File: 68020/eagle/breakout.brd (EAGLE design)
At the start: 50 x 49.9 mm, 5 parts, among them IC1 MC68020

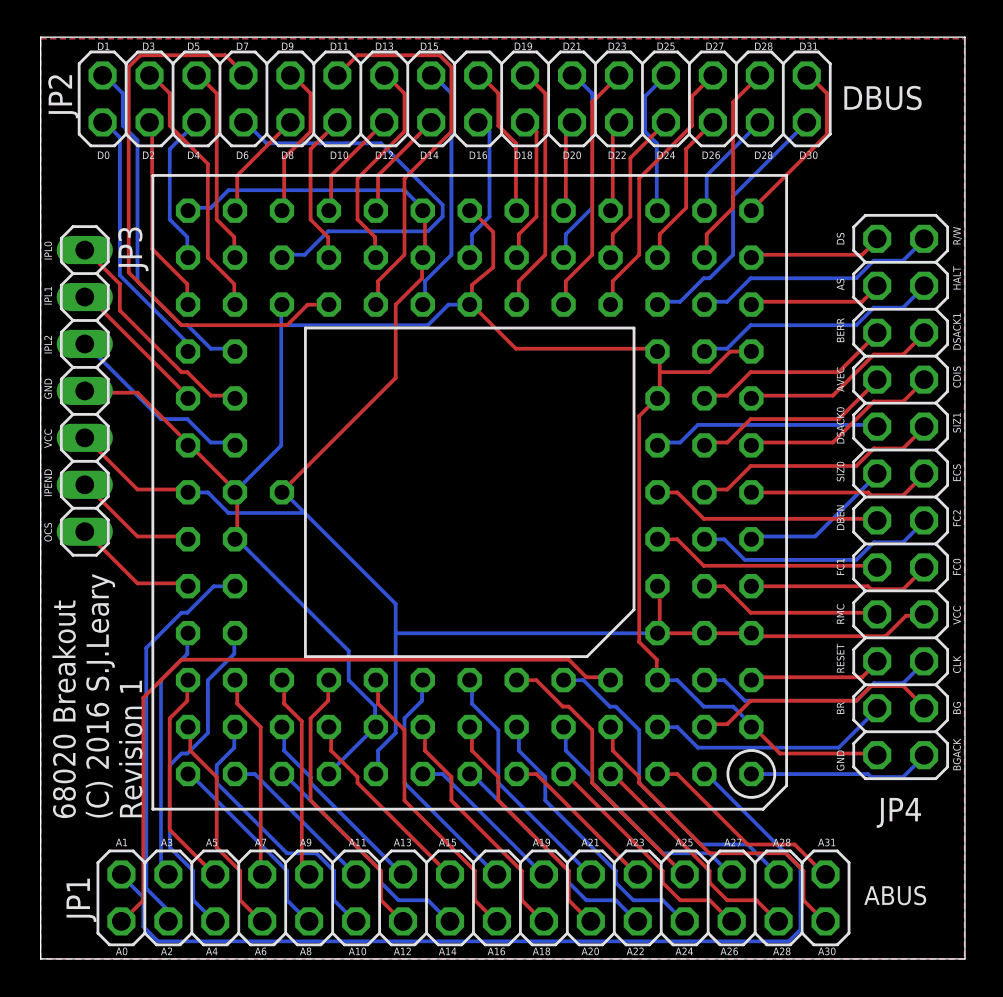
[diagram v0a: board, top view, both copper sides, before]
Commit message: refactored 68020 breakout board to be a mirror of the 030 board... means they can mate. Added an unrouted shunt for the 68k
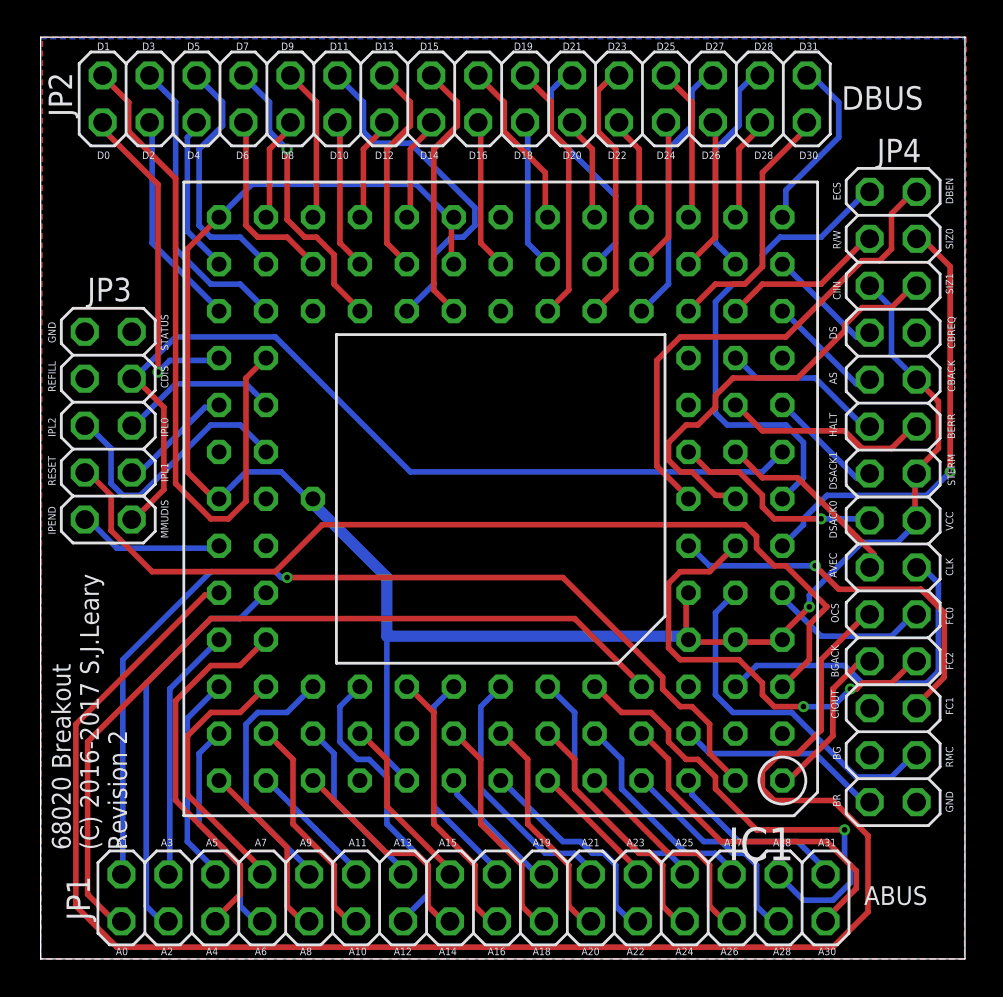
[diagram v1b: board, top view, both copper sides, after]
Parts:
- IC1: value MC68020 -> (none)
- JP3: value IPL BUS -> (none); device pinhead:1X07 -> pinhead:2X05
- JP4: device pinhead:2X12 -> pinhead:2X14
- moved JP3 2.27 mm to (3.66, 28.9)
- moved IC1 1.71 mm to (24.9, 24.9)
- moved JP4 0.41 mm to (46.1, 25.0)
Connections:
- new net BG: IC1.B02
- new net CBREQ: JP4.8
- new net CIIOUT: JP4.23
- new net REFILL: JP3.3
- new net STATUS: JP3.2
- net AS20: now also JP4.9; no longer JP4.3
- net AVEC: now also JP4.17; no longer JP4.7
- net BERR: now also JP4.12; no longer JP4.5
- net BG20: now also JP4.25; no longer IC1.B02, JP4.22
- net BGACK: now also JP4.21; no longer JP4.24
- net BR: now also JP4.27; no longer JP4.21
- net CDIS: now also JP3.10, JP3.4; no longer JP4.8
- net CLK20: now also JP4.18; no longer JP4.20
- net DBEN: now also JP4.2; no longer JP4.13
- net DS20: now also JP4.7; no longer JP4.1
- net DSACK0: now also JP4.15; no longer JP4.9
- net DSACK1: now also JP4.13; no longer JP4.6
- net ECS: now also JP4.1; no longer JP4.12
- net FC0: now also JP4.20; no longer JP4.16
- net FC1: now also JP4.24; no longer JP4.15
- net FC2: now also JP4.22; no longer JP4.14
- net GND: now also JP3.1, JP4.28; no longer JP3.4, JP4.23
- net HALT: now also JP4.11; no longer JP4.4
- net IPEND: now also JP3.9; no longer JP3.6
- net IPL0: now also JP3.6; no longer JP3.1
- net IPL1: now also JP3.8; no longer JP3.2
- net IPL2: now also JP3.5; no longer JP3.3
- net OCS: now also JP4.19; no longer JP3.7
- net R/W: now also JP4.3; no longer JP4.2
- net RESET: now also JP3.7; no longer JP4.19
- net RMC: now also JP4.26; no longer JP4.17
- net SIZ0: now also JP4.4; no longer JP4.11
- net SIZ1: now also JP4.6; no longer JP4.10
- net VCC: now also JP4.10, JP4.14, JP4.16, JP4.5; no longer JP3.5, JP4.18
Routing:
- net GND: track 107.4 -> 0.00 mm
- net OCS: track 6.85 -> 88.6 mm
- net RESET: track 7.26 -> 52.1 mm
- net CDIS: track 10.9 -> 48.9 mm
- net D1: track 18.9 -> 36.9 mm
- net ECS: track 9.93 -> 26.2 mm
- net SIZ0: track 8.32 -> 24.5 mm, vias 0 -> 1
- net D7: track 30.6 -> 15.7 mm, vias 0 -> 1
- net DBEN: track 12.6 -> 27.2 mm
- net BG20: track 13.3 -> 0.00 mm
- net D6: track 22.9 -> 10.1 mm
- net VCC: track 96.0 -> 107.3 mm, vias 0 -> 1
- net FC2: track 13.3 -> 24.2 mm, vias 0 -> 2
- net SIZ1: track 13.4 -> 23.0 mm
- net RMC: track 10.0 -> 19.3 mm
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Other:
- board text added: "68020 Breakout (C) 2016-2017 S.J.Leary Revision 2"
- board text added: "CBACK"
- board text added: "CBREQ"
- board text added: "CIIN"
- board text added: "CIOUT"
- board text added: "MMUDIS"
- board text added: "REFILL"
- board text added: "STATUS"
- board text added: "STERM"
- board text removed: "68020 Breakout (C) 2016 S.J.Leary Revision 1"
